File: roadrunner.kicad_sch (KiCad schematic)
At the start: 1 part, among them U1 ESP32-C6-MINI-1

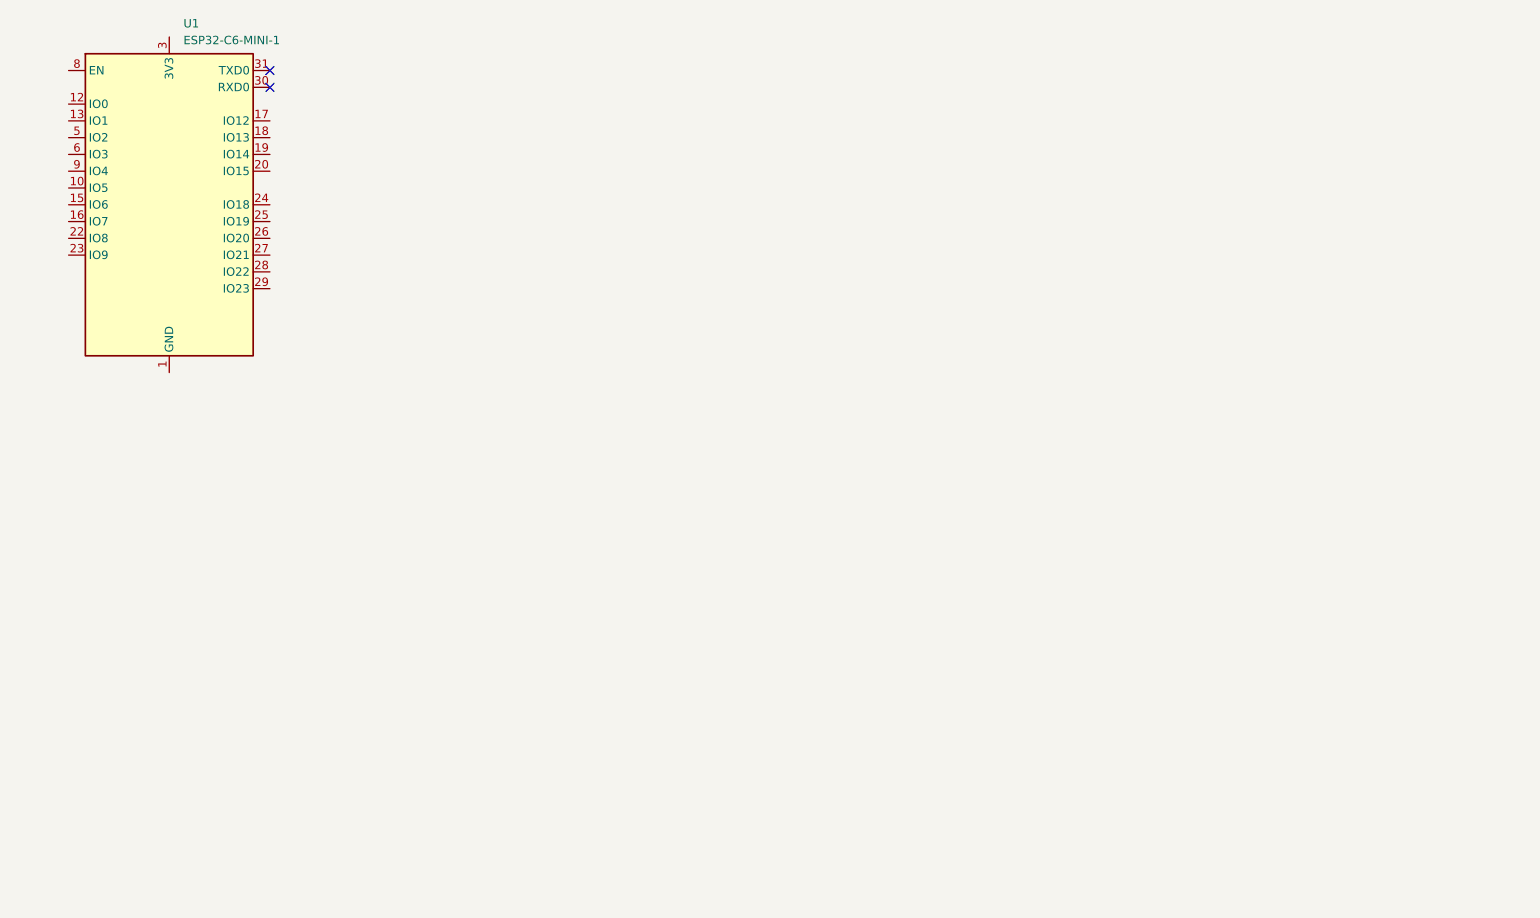
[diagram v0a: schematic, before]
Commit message: Added basic components
Put in ESP32, Audio Amplifier, and connectors for Visual and Sensing
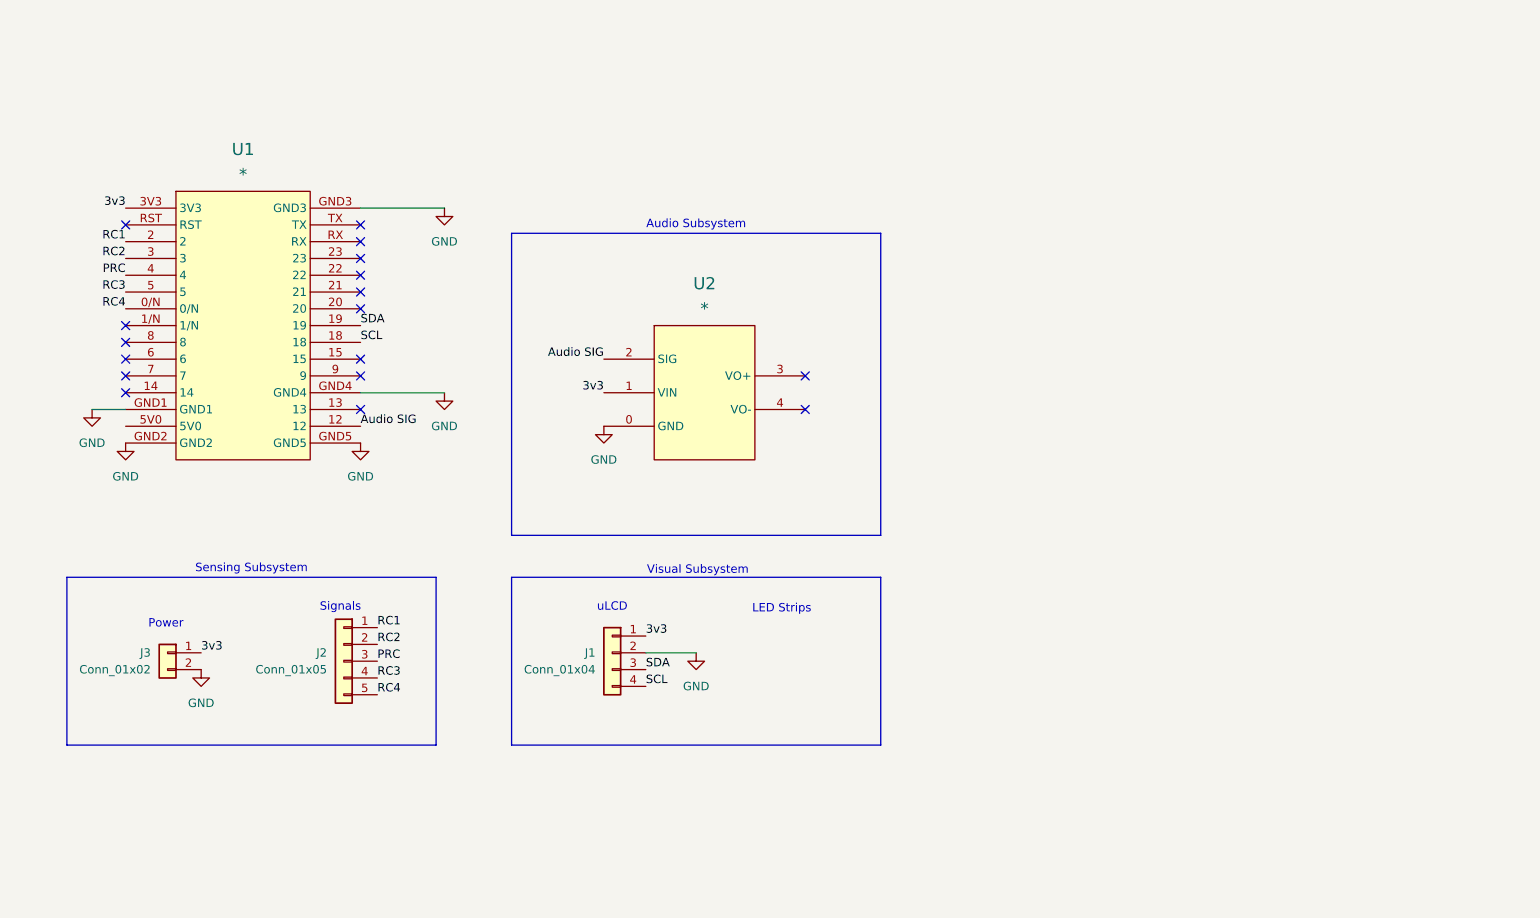
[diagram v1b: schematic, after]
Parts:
- removed U1: ESP32-C6-MINI-1, RF_Module:ESP32-C6-MINI-1, symbol RF_Module:ESP32-C6-MINI-1
- added J1: Conn_01x04, Connector_JST:JST_EH_B4B-EH-A_1x04_P2.50mm_Vertical, symbol Connector_Generic:Conn_01x04
- added J2: Conn_01x05, Connector_JST:JST_EH_B5B-EH-A_1x05_P2.50mm_Vertical, symbol Connector_Generic:Conn_01x05
- added J3: Conn_01x02, Connector_JST:JST_EH_B2B-EH-A_1x02_P2.50mm_Vertical, symbol Connector_Generic:Conn_01x02
- added U1: *, ESP32, symbol Components_3011:ESP32
- added U2: *, Components_3011:Adafruit_PAM8904, symbol Components_3011:PAM8904
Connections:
- new net 3v3: J1.1 (Pin_1), J3.1 (Pin_1), U1.3V3, U2.1 (VIN)
- new net Audio SIG: U1.12, U2.2 (SIG)
- new net GND: J1.2 (Pin_2), J3.2 (Pin_2), U1.GND1, U1.GND2, U1.GND3, U1.GND4, U1.GND5, U2.0 (GND)
- new net PRC: J2.3 (Pin_3), U1.4
- new net RC1: J2.1 (Pin_1), U1.2
- new net RC2: J2.2 (Pin_2), U1.3
- new net RC3: J2.4 (Pin_4), U1.5
- new net RC4: J2.5 (Pin_5), U1.0/N
- new net SCL: J1.4 (Pin_4), U1.18
- new net SDA: J1.3 (Pin_3), U1.19
- no-connect marks 2 -> 17
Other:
- note added: "Audio Subsystem"
- note added: "LED Strips"
- note added: "Power"
- note added: "Sensing Subsystem"
- note added: "Signals"
- note added: "Visual Subsystem"
- note added: "uLCD"

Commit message: Updated some pins
Updates some of the schematic changes that I had tested on the breadboard.
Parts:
- added BOTTOM, LEFT, RIGHT, TOP: LED, symbol Device:LED
- added R220 (x4): R, Package_DIP:DIP-8_W7.62mm, symbol Device:R
- added U3: L293D, Package_DIP:DIP-16_W7.62mm, symbol Driver_Motor:L293D
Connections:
- net 3v3: no longer J1.1 (Pin_1)
- net GND: now also J1.4 (Pin_4), BOTTOM.1 (K), LEFT.1 (K), RIGHT.1 (K), TOP.1 (K); no longer J1.2 (Pin_2)
- net PRC: no longer U1.4
- net RC1: now also U1.23; no longer U1.2
- net RC2: now also U1.22; no longer U1.3
- net RC3: now also U1.21; no longer U1.5
- net RC4: now also U1.20; no longer U1.0/N
- net SCL: now also J1.2 (Pin_2), U1.7; no longer J1.4 (Pin_4), U1.18
- net SDA: now also J1.1 (Pin_1), U1.8; no longer J1.3 (Pin_3), U1.19
- new net: R220.1, TOP.2 (A)
- new net: LEFT.2 (A), R220.1
- new net: BOTTOM.2 (A), R220.1
- new net: R220.1, RIGHT.2 (A)
- new net 3V3: J1.3 (Pin_3)
- new net B: R220.2, U1.4
- new net L: R220.2, U1.5
- new net R: R220.2, U1.2
- new net RC5: U1.19
- new net T: R220.2, U1.3
- no-connect marks 17 -> 13
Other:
- note added: "Motion Subsystem"

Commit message: Added power subsystem
Added in power switch and buck converter
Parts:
- removed BOTTOM, LEFT, RIGHT, TOP: LED, symbol Device:LED
- removed R220 (x4): R, Package_DIP:DIP-8_W7.62mm, symbol Device:R
- added C1, C2: 0.1uF, Capacitor_SMD:C_1206_3216Metric_Pad1.33x1.80mm_HandSolder, symbol Device:C_Small
- added J4: Conn_01x03, Connector_JST:JST_XH_B3B-XH-A_1x03_P2.50mm_Vertical, symbol Connector_Generic:Conn_01x03
- added J5: Conn_01x02, Connector_JST:JST_XH_B2B-XH-A_1x02_P2.50mm_Vertical, symbol Connector_Generic:Conn_01x02
- added SW101: SW_SPDT, Microtransat:SW_EG1218, symbol Switch:SW_SPDT
- added U4: *, ADA4683_MPM3610_BREAKOUT, symbol Components_3011:MPM3610 3V3 Breakout
- J1: footprint Connector_JST:JST_EH_B4B-EH-A_1x04_P2.50mm_Vertical -> Connector_JST:JST_XH_B4B-XH-A_1x04_P2.50mm_Vertical
- J2: footprint Connector_JST:JST_EH_B5B-EH-A_1x05_P2.50mm_Vertical -> Connector_JST:JST_XH_B5B-XH-A_1x05_P2.50mm_Vertical
- J3: footprint Connector_JST:JST_EH_B2B-EH-A_1x02_P2.50mm_Vertical -> Connector_JST:JST_XH_B2B-XH-A_1x02_P2.50mm_Vertical
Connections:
- net B is gone; now on net PRC: U1.4
- net L is gone; now on net RC3: U1.5
- net R is gone; now on net RC1: U1.2
- net T is gone; now on net RC2: U1.3
- net 3v3: now also U3.1 (EN1,2), U3.9 (EN3,4)
- net GND: now also U3.12 (GND), U3.13 (GND), U3.4 (GND), U3.5 (GND), C1.2, C2.2, J5.2 (Pin_2), U4.4 (GND)
- net RC1: no longer U1.23
- net RC2: no longer U1.22
- net RC3: no longer U1.21
- net RC4: now also U1.0/N; no longer U1.20
- net 3A: now reaches U3.10 (3A)
- net 3A: now also U1.21
- net 4A: now reaches U3.15 (4A)
- net 4A: now also U1.20
- net 5V: now reaches U3.16 (VCC1)
- net 5V: now also U1.5V0, U3.8 (VCC2), C1.1, C2.1, U4.3 (5V)
- net 1A: now reaches U3.2 (1A)
- net 1A: now also U1.23
- net 2A: now reaches U3.7 (2A)
- net 2A: now also U1.22
- net RC5: no longer names the net of U1.19
- new net: SW101.2 (B), U4.2 (VIN)
- new net: J5.1 (Pin_1), SW101.1 (A)
- no-connect marks 13 -> 14
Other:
- note added: "Buck Converter"
- note added: "MAKE SURE WE HAVE"
- note added: "Power Subsystem"
- moved on the sheet: U3

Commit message: update Halloween
update fixing all errors. Waiting to add libraries for the components (4 still missing).
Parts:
- added J6: Conn_01x04, symbol Connector_Generic:Conn_01x04
- J5: footprint Connector_JST:JST_XH_B2B-XH-A_1x02_P2.50mm_Vertical -> (none)
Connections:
- net 3v3 is gone; now on net 3V3: J3.1 (Pin_1), U1.3V3, U2.1 (VIN), U3.1 (EN1,2), U3.9 (EN3,4)
- net 5V: now also J4.3 (Pin_3)
- net GND: now also J4.1 (Pin_1)
- net at U3.11 (3Y): now also J6.3 (Pin_3)
- net at U3.14 (4Y): now also J6.4 (Pin_4)
- net at U3.3 (1Y): now also J6.1 (Pin_1)
- net at U3.6 (2Y): now also J6.2 (Pin_2)
- net AUDIO_SIG: now reaches U1.14
- net AUDIO_SIG: now also U2.2 (SIG)
- net LED_DS: now reaches U1.18
- net LED_DS: now also J4.2 (Pin_2)
- net Audio SIG: no longer names the net of U1.12
- net Audio SIG: no longer U2.2 (SIG)
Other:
- moved on the sheet: J4
